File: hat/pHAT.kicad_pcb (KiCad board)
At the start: 2 copper layers, 65 x 30 mm, 8 parts, among them U3 HATconnector

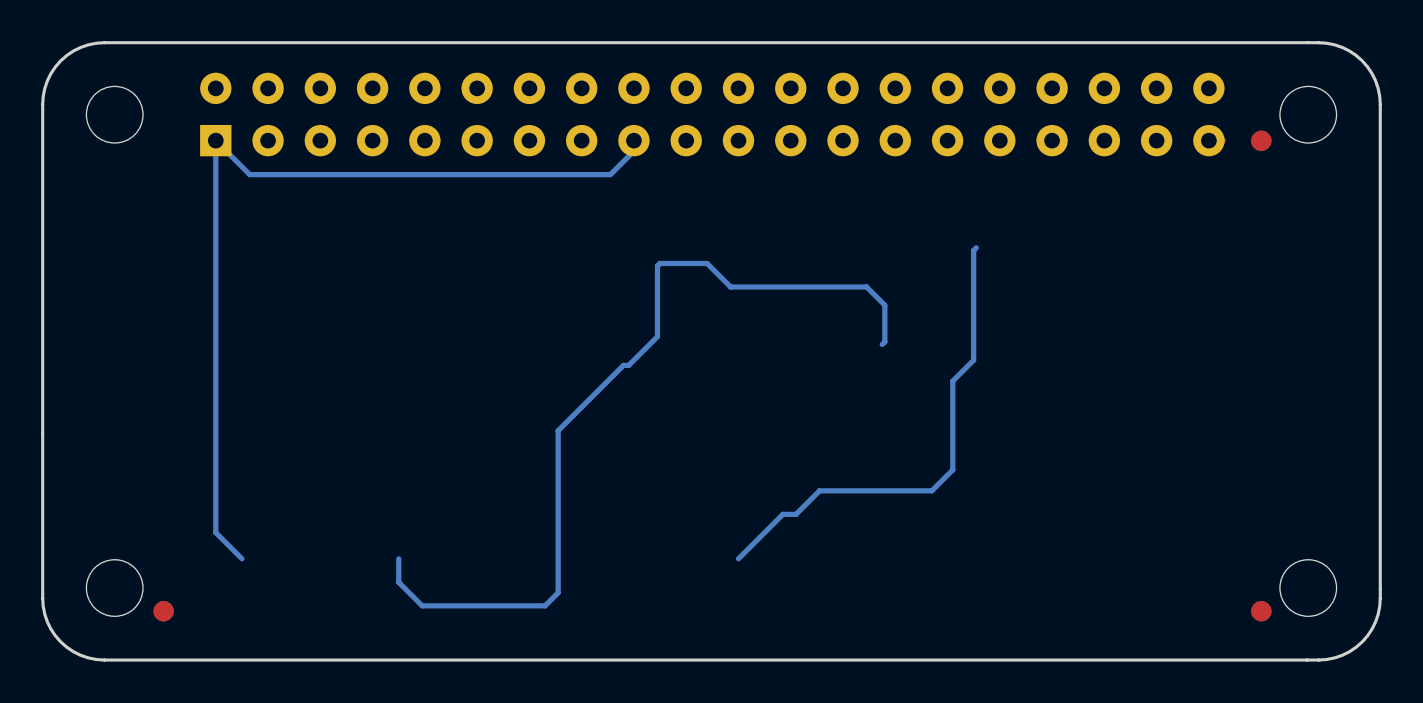
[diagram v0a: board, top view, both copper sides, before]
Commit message: Adding Loginator (port from Eagle)
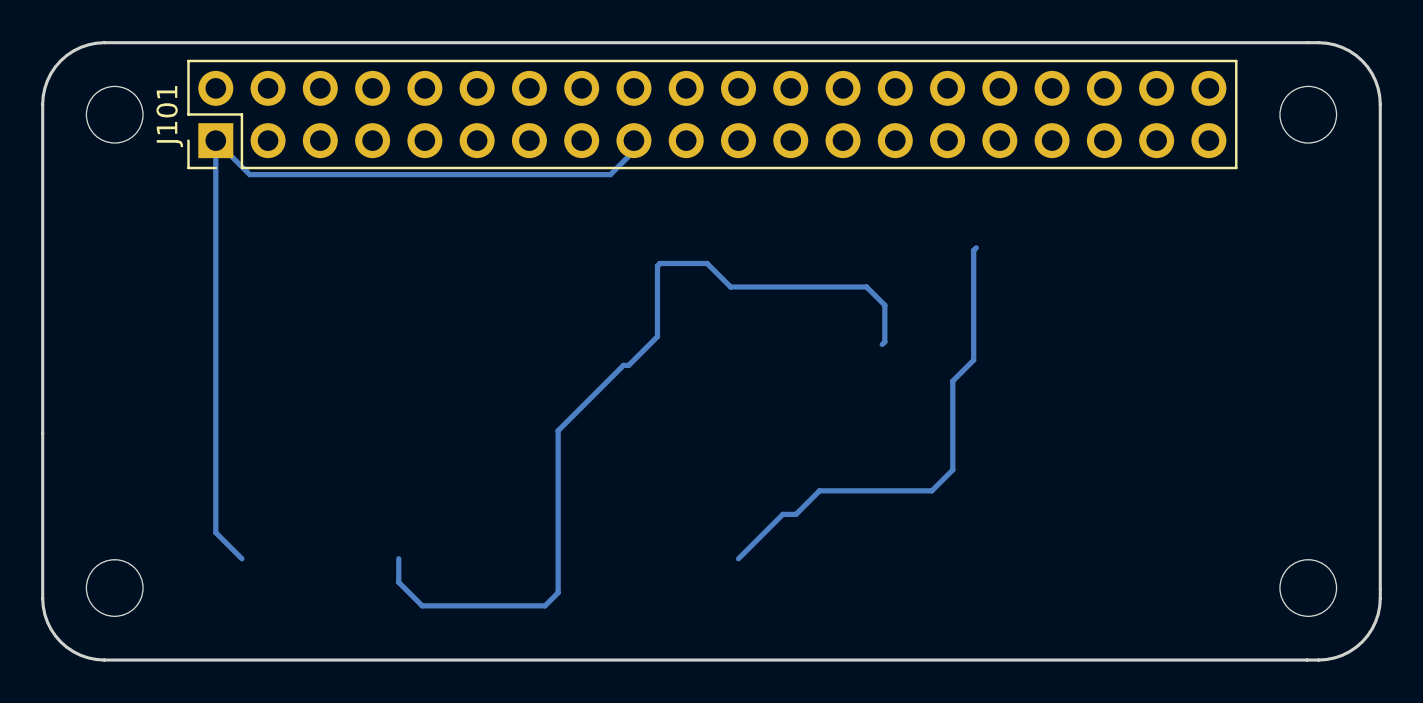
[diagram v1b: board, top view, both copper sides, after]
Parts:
- removed FID1, FID2, FID3: FIDUCIAL, DiscoCap:FIDUCIAL
- removed U3: HATconnector, Power:PHAT
- added J101: RPi_GPIO, Pin_Headers:Pin_Header_Straight_2x20_Pitch2.54mm, F.Cu at (117.9, 84.3)
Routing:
- net Net-(J101-Pad39): track 0.00 -> 0.76 mm
- net GND: track 1.58 -> 0.81 mm
